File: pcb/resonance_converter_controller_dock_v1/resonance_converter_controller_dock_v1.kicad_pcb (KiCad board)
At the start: 2 copper layers, 157 parts, among them J1 FX18-120S-0.8SV15, J10 Conn_Coaxial, J11 Conn_01x02, J12 Conn_01x02, J13 Conn_Coaxial, J14 Conn_Coaxial, J15 Conn_01x02, J16 Conn_01x02, J17 Conn_Coaxial, J18 Conn_01x02, J19 Conn_01x04, J2 Conn_01x52_MountingPin, J20 Conn_01x04, J21 Conn_01x04, J22 Conn_01x06, J23 Conn_Coaxial, J24 Conn_01x02, J25 Conn_01x02, J26 Conn_Coaxial, J27 Conn_01x04, J28 Conn_01x02, J29 USB_C_Receptacle_USB2.0_14P, J3 Conn_Coaxial, J30 Conn_01x09, J31 Conn_01x04_MountingPin, J32 Conn_01x04_MountingPin, J33 Conn_01x04_MountingPin, J34 Conn_02x05_Odd_Even, J4 Conn_01x02, J5 Conn_Coaxial, J6 Conn_01x02, J7 Conn_Coaxial, J8 Conn_01x02, J9 Conn_Coaxial, M1 Fan_4pin, SW1 RotaryEncoder_Switch_MP, SW2 SW_SPST, SW3 SW_SPST, SW4 SW_SPST, SW5 SW_SPST, SW6 SW_SPST, U1 STM32F105R8Tx, U10 TMUX131RMG, U11 TMUX131RMG, U12 TMUX131RMG, U13 TMUX131RMG, U14 TMUX131RMG, U15 TMUX154ERSW, U16 AT24CS32-XHM, U17 TMUX1574RSV, U18 TMUX1574RSV, U19 TMUX131RMG, U2 FUSB302B01MPX, U20 TMUX1574RSV, U21 TMUX154ERSW, U22 TMUX154ERSW, U23 TMUX154ERSW, U24 BTS5012SDA, U25 BTS5012SDA, U26 BTS5012SDA, U27 74LVC1G04, U3 LM2576HVS-ADJ, U4 TMUX131RMG, U5 LM7812_TO220, U6 TPS2116DRL, U7 AZ1117-3.3, U8 AP2171W, U9 TMUX131RMG, Y1 16Mhz

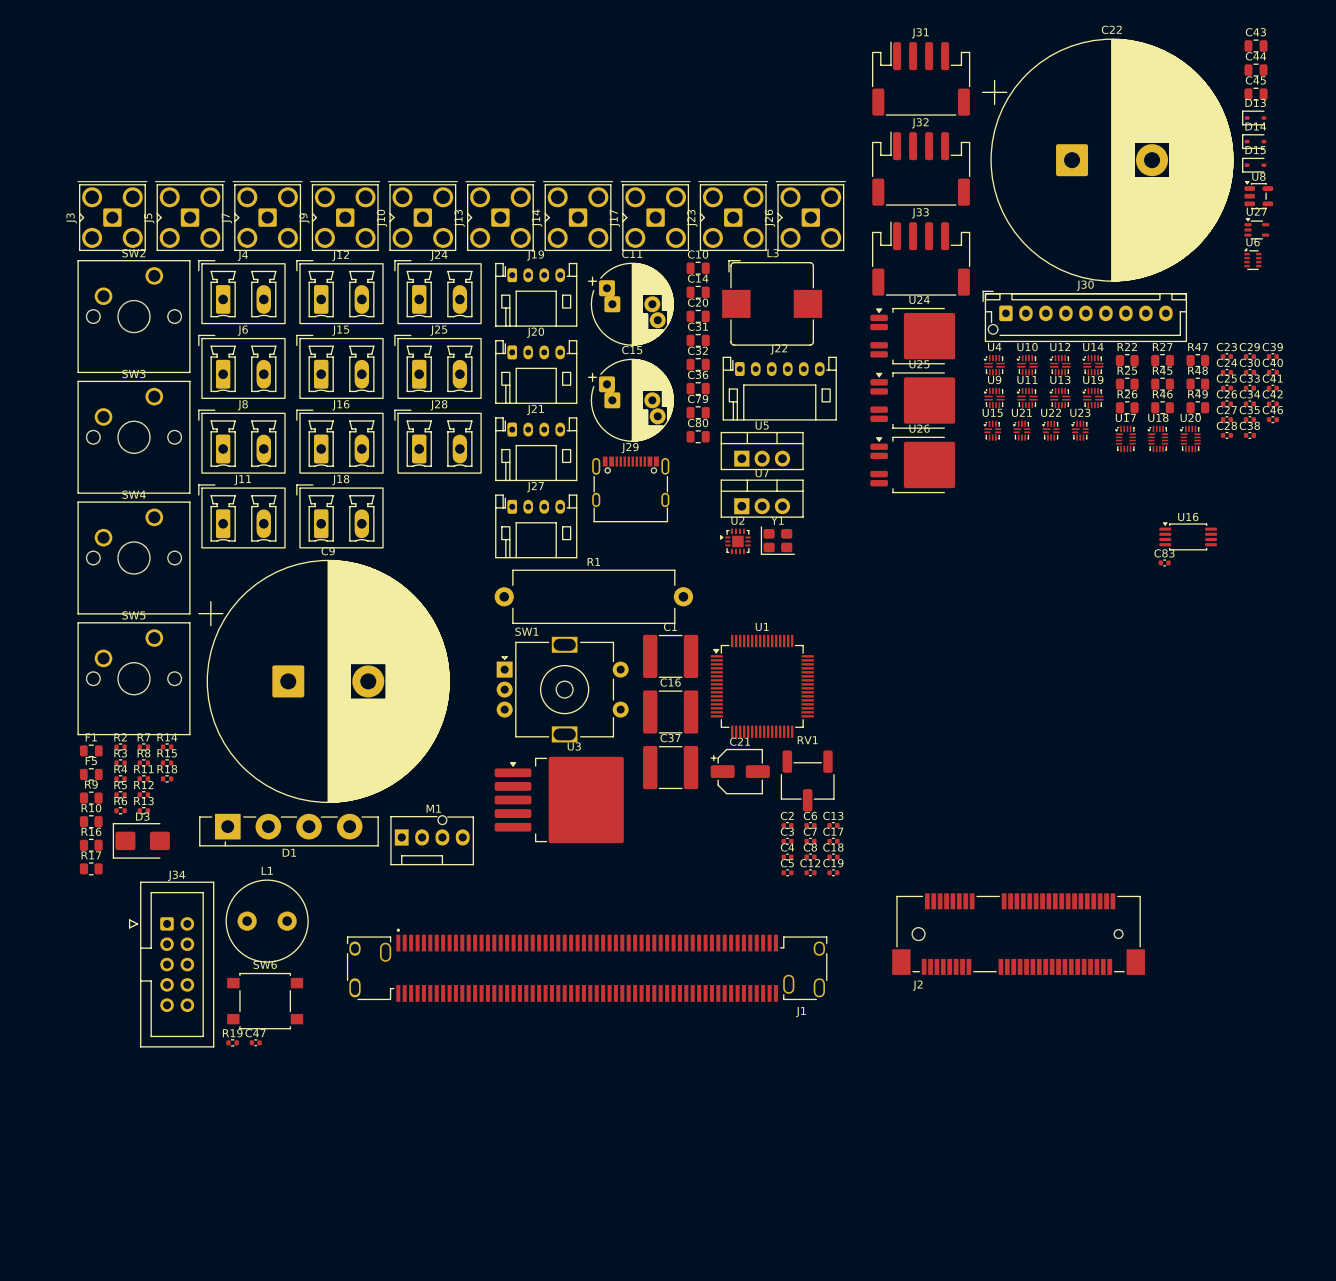
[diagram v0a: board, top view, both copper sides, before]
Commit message: Fix errors and make initial component placement in dock
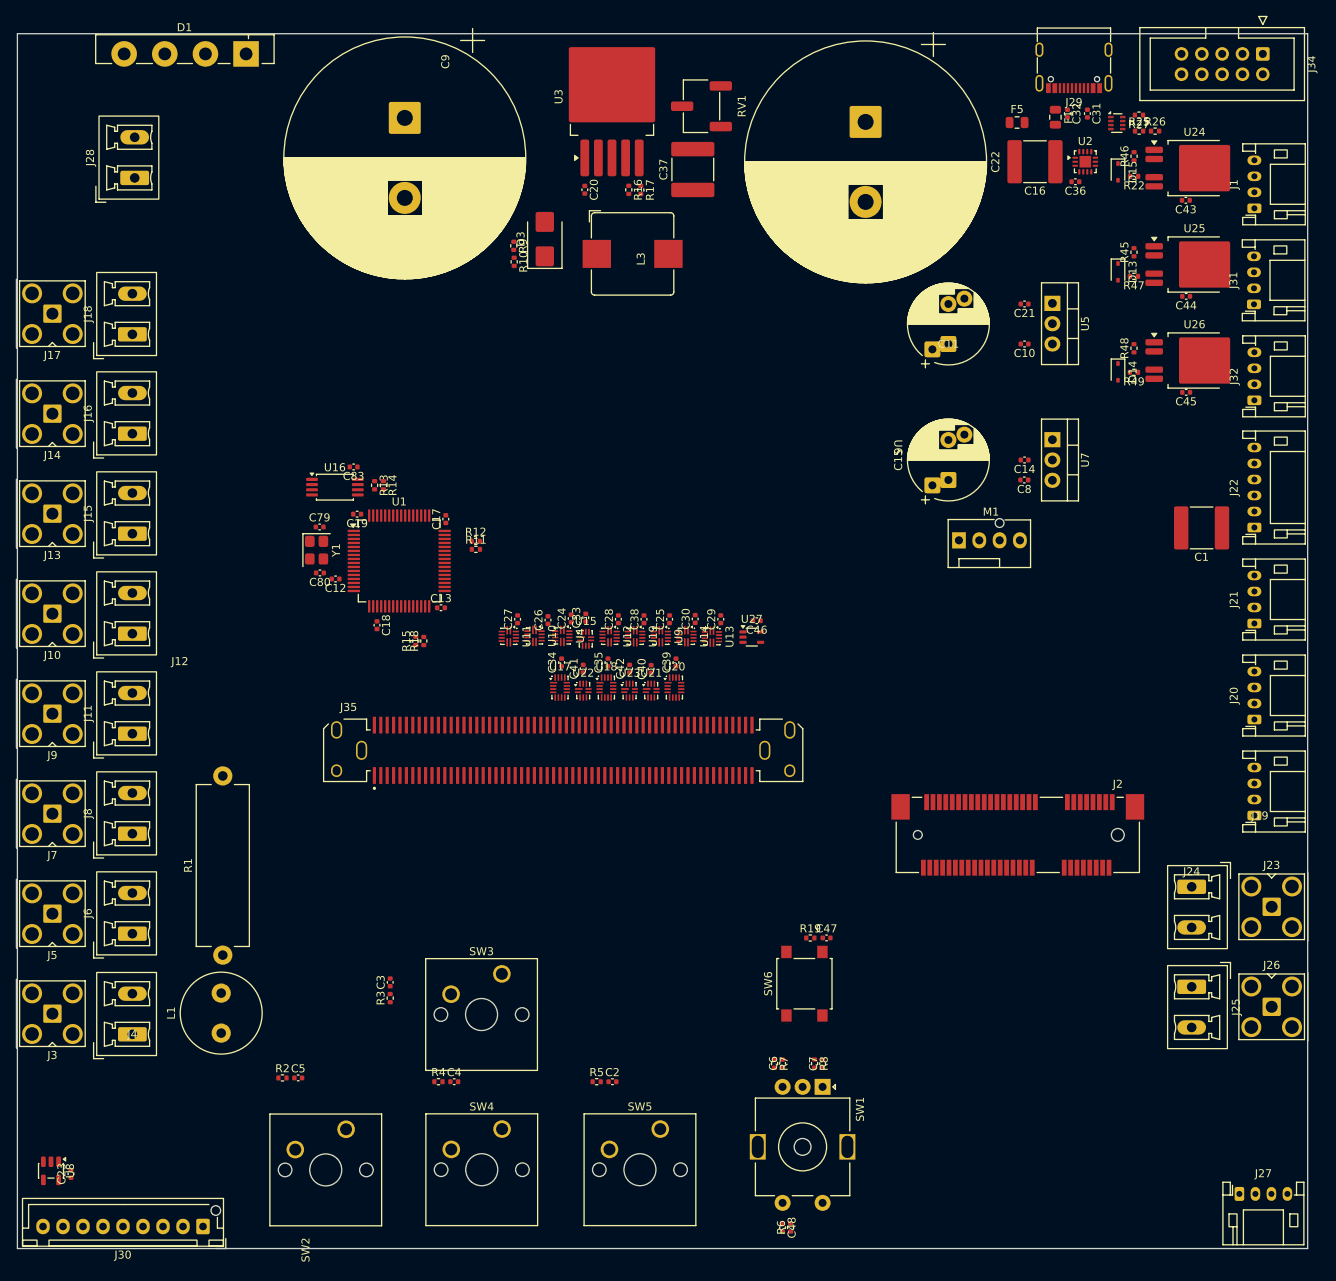
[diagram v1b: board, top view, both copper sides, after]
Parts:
- removed J33: Conn_01x04_MountingPin, Connector_JST:JST_PH_S4B-PH-SM4-TB_1x04-1MP_P2.00mm_Horizontal
- added C48: 100nF, Capacitor_SMD:C_0402_1005Metric, F.Cu at (178.8, 173.4)
- added J35: FX18-120P-0.8SV, FX18-120P-0.8SV:HIROSE_FX18-120P-0.8SV, F.Cu at (151.4, 113.7)
- C10, C14, C20, C31, C32, C36, C43, C44, C45, C79, C80: footprint Capacitor_SMD:C_0805_2012Metric -> Capacitor_SMD:C_0402_1005Metric
- C21: value C_Polarized -> C; footprint Capacitor_SMD:CP_Elec_5x4.5 -> Capacitor_SMD:C_0402_1005Metric
- C8: value 100nF -> C
- J1: value FX18-120S-0.8SV15 -> Conn_01x04; footprint FX18-120S-0.8SV15:HIROSE_FX18-120S-0.8SV15 -> Connector_JST:JST_PH_S4B-PH-K_1x04_P2.00mm_Horizontal
- J31, J32: value Conn_01x04_MountingPin -> Conn_01x04; footprint Connector_JST:JST_PH_S4B-PH-SM4-TB_1x04-1MP_P2.00mm_Horizontal -> Connector_JST:JST_PH_S4B-PH-K_1x04_P2.00mm_Horizontal
- R10, R16, R17, R22, R25, R26, R27, R45, R46, R47, R48, R49, R9: footprint Resistor_SMD:R_0805_2012Metric -> Resistor_SMD:R_0402_1005Metric
- moved U8 194.0 mm to (87.4, 166.3), turned to -90 degrees
- moved C23 177.0 mm to (89.9, 166.6), turned to 90 degrees
- moved J34 174.9 mm to (238.8, 26.6), turned to -90 degrees
- moved J30 152.0 mm to (106.4, 173.2), turned to 180 degrees
- moved F1 144.2 mm to (212.9, 34.6), turned to -90 degrees
- moved F5 141.5 mm to (208.1, 35.2)
- moved J1 126.4 mm to (237.8, 46.0), turned to 90 degrees
- moved J27 125.1 mm to (235.9, 169.2)
- moved J25 123.2 mm to (230.0, 143.3), turned to -90 degrees
- moved J24 121.3 mm to (230.0, 130.8), turned to -90 degrees
- moved J19 114.8 mm to (237.8, 121.8), turned to 90 degrees
- moved J26 114.2 mm to (240.0, 145.8), turned to -90 degrees
- moved SW2 109.3 mm to (124.3, 161.1)
- moved J23 109.3 mm to (240.0, 133.3), turned to -90 degrees
- moved R17 109.2 mm to (161.1, 43.7), turned to -90 degrees
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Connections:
- C12 pad 1: Net-(C12-Pad1) -> +3.3V
- C13 pad 1: Net-(C12-Pad1) -> +3.3V
- C17 pad 1: Net-(C12-Pad1) -> +3.3V
- C18 pad 1: Net-(C12-Pad1) -> +3.3V
- C19 pad 1: Net-(C12-Pad1) -> +3.3V
- C21 pad 1: Net-(D1-+) -> VBUS_DOCK
- C8 pad 1: Net-(D1-+) -> +12V
- J1 pad 1: GND -> Net-(J1-Pin_1)
- J1 pad 2: GND -> +3.3V
- J1 pad 3: OCD_IN -> +12V
- R45 pad 2: Net-(J32-Pin_1) -> Net-(J31-Pin_1)
- R46 pad 2: Net-(J31-Pin_1) -> Net-(J1-Pin_1)
- R48 pad 2: Net-(J33-Pin_1) -> Net-(J32-Pin_1)
- U10 pad 7: SOMLCD_SCK -> SOM_LCD_SCK
- U24 pad 1: Net-(J31-Pin_1) -> Net-(J1-Pin_1)
- U24 pad 5: Net-(J31-Pin_1) -> Net-(J1-Pin_1)
- U25 pad 1: Net-(J32-Pin_1) -> Net-(J31-Pin_1)
- U25 pad 5: Net-(J32-Pin_1) -> Net-(J31-Pin_1)
- U26 pad 1: Net-(J33-Pin_1) -> Net-(J32-Pin_1)
- U26 pad 5: Net-(J33-Pin_1) -> Net-(J32-Pin_1)
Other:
- board outline added: 161.3 x 151.8 mm

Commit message: Add mounting holes and some rework
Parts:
- added C49: C, Capacitor_SMD:C_2220_5750Metric, F.Cu at (141.8, 124.7)
- added C50: C_Polarized, Capacitor_THT:CP_Radial_D10.0mm_P5.00mm_P7.50mm, F.Cu at (115.0, 77.5)
- added C51: C, Capacitor_SMD:C_2220_5750Metric, F.Cu at (139.0, 102.4)
- added H1: MountingHole_Pad, MountingHole:MountingHole_3.2mm_M3_Pad_Via, F.Cu at (88.2, 47.6)
- added H2: MountingHole_Pad, MountingHole:MountingHole_3.2mm_M3_Pad_Via, F.Cu at (230.6, 28.5)
- added H3: MountingHole_Pad, MountingHole:MountingHole_3.2mm_M3_Pad_Via, F.Cu at (229.0, 171.0)
- added H4: MountingHole_Pad, MountingHole:MountingHole_3.2mm_M3_Pad_Via, F.Cu at (88.2, 164.3)
- added R20: R, Resistor_THT:R_Axial_Power_L20.0mm_W6.4mm_P22.40mm, F.Cu at (106.2, 140.4)
- added R21: R, Resistor_THT:R_Axial_Power_L20.0mm_W6.4mm_P22.40mm, F.Cu at (106.2, 133.3)
- U5, U7: footprint Package_TO_SOT_THT:TO-220-3_Vertical -> Package_TO_SOT_SMD:TO-263-2
- moved C47 113.2 mm to (232.8, 34.8)
- moved R19 113.2 mm to (230.8, 34.8)
- moved SW6 113.2 mm to (230.0, 40.5)
- moved R26 106.3 mm to (144.8, 105.7), turned to 90 degrees
- moved R25 106.2 mm to (144.8, 107.7), turned to 90 degrees
- moved R27 102.1 mm to (150.7, 106.0), turned to 90 degrees
- moved U6 101.7 mm to (147.9, 106.4)
- moved C79 64.8 mm to (176.3, 52.0), turned to -90 degrees
- moved Y1 64.5 mm to (173.4, 51.6), turned to 180 degrees
- moved U16 64.0 mm to (183.5, 60.3), turned to -90 degrees
- moved C80 63.3 mm to (170.5, 52.0), turned to 90 degrees
- moved C83 62.7 mm to (186.0, 62.7), turned to 90 degrees
- moved C19 58.5 mm to (177.9, 57.8), turned to 90 degrees
- moved C12 58.4 mm to (168.6, 55.9)
- moved R13 57.9 mm to (183.7, 65.3), turned to 180 degrees
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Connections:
- net Net-(U1-PA11) renamed /PUSB-
- net Net-(U1-PA12) renamed /PUSB+
- C6 pad 1: DOCK_ENCODER_CHB -> DEV_ENCODER_B
- C7 pad 1: DOCK_ENCODER_CHA -> DEV_ENCODER_A
- C8 pad 1: +12V -> VBUS_DOCK
- J27 pad 1: VCC -> +3.3V
- R2 pad 1: VCC -> +3.3V
- R3 pad 1: VCC -> +3.3V
- R4 pad 1: VCC -> +3.3V
- R5 pad 1: VCC -> +3.3V
- R6 pad 1: VCC -> +3.3V
- R7 pad 1: VCC -> +3.3V
- R7 pad 2: DOCK_ENCODER_CHB -> DEV_ENCODER_B
- R8 pad 1: VCC -> +3.3V
- R8 pad 2: DOCK_ENCODER_CHA -> DEV_ENCODER_A
- SW1 pad A: DOCK_ENCODER_CHA -> DEV_ENCODER_A
- SW1 pad B: DOCK_ENCODER_CHB -> DEV_ENCODER_B
- U1 pad 10: PAD_FWD_REMOTE -> CTRL_RXTX_FWD_REMOTE
- U1 pad 35: /PAD_BUS_SELECT_0 -> /PAD_BUS_SELECT_1
- U1 pad 36: /PAD_BUS_SELECT_1 -> /PAD_BUS_SELECT_0
- U1 pad 37: /ENCODER_BUS_SELECT_0 -> /ENCODER_BUS_SELECT_1
- U1 pad 38: /ENCODER_BUS_SELECT_1 -> /ENCODER_BUS_SELECT_0
- U1 pad 39: /LCD_BUS_SELECT_0 -> /LCD_BUS_SELECT_1
- U1 pad 40: /LCD_BUS_SELECT_1 -> /LCD_BUS_SELECT_0
- U1 pad 9: CTRL_RXTX_FWD_REMOTE -> PAD_FWD_REMOTE
- U15 pad 1: SOM_CTRL_TX -> SOM_CTRL_RX
- U15 pad 2: FROM_REMOTE_CTRL_TX -> FROM_REMOTE_CTRL_RX
- U15 pad 3: DEV_CTRL_TX -> DEV_CTRL_RX
- U15 pad 5: DEV_CTRL_RX -> DEV_CTRL_TX
- U15 pad 6: FROM_REMOTE_CTRL_RX -> FROM_REMOTE_CTRL_TX
- U15 pad 7: SOM_CTRL_RX -> SOM_CTRL_TX
- U17 pad 1: TO_REMOTE_LCD_MOSI -> TO_REMOTE_LCD_SS
- U17 pad 10: DOCK_LCD_SS -> DOCK_LCD_MOSI
- U17 pad 11: TO_REMOTE_LCD_SS -> TO_REMOTE_LCD_MOSI
- U17 pad 12: SOM_LCD_SS -> SOM_LCD_MOSI
- U17 pad 16: SOM_LCD_MOSI -> SOM_LCD_SS
- U17 pad 2: DOCK_LCD_MOSI -> DOCK_LCD_SS
- U18 pad 3: SOM_LCD_DC -> SOM_LCD_BL
- U18 pad 4: TO_REMOTE_LCD_DC -> TO_REMOTE_LCD_BL
- U18 pad 5: DOCK_LCD_DC -> DOCK_LCD_BL
- U18 pad 7: DOCK_LCD_BL -> DOCK_LCD_DC
- U18 pad 8: TO_REMOTE_LCD_BL -> TO_REMOTE_LCD_DC
- U18 pad 9: SOM_LCD_BL -> SOM_LCD_DC
- U20 pad 1: TO_REMOTE_PAD_UP -> TO_REMOTE_PAD_RIGHT
- U20 pad 10: DOCK_GPIO3 -> DOCK_GPIO0
- U20 pad 11: TO_REMOTE_PAD_RIGHT -> TO_REMOTE_PAD_UP
- U20 pad 12: SOM_PAD_RIGHT -> SOM_PAD_UP
- U20 pad 14: unconnected-(U20-VDD-Pad14) -> +3.3V
- U20 pad 16: SOM_PAD_UP -> SOM_PAD_RIGHT
- U20 pad 2: DOCK_GPIO0 -> DOCK_GPIO3
- U20 pad 3: SOM_PAD_DOWN -> SOM_PAD_LEFT
- U20 pad 4: TO_REMOTE_PAD_DOWN -> TO_REMOTE_PAD_LEFT
- U20 pad 5: DOCK_GPIO1 -> DOCK_GPIO2
- U20 pad 7: DOCK_GPIO2 -> DOCK_GPIO1
- U20 pad 8: TO_REMOTE_PAD_LEFT -> TO_REMOTE_PAD_DOWN
- U20 pad 9: SOM_PAD_LEFT -> SOM_PAD_DOWN
- U22 pad 1: SOM_CTRL_TX -> SOM_CTRL_RX
- U22 pad 2: TO_REMOTE_CTRL_TX -> TO_REMOTE_CTRL_RX
- U22 pad 3: DOCK_CTRL_TX -> DOCK_CTRL_RX
- U22 pad 5: DOCK_CTRL_RX -> DOCK_CTRL_TX
- U22 pad 6: TO_REMOTE_CTRL_RX -> TO_REMOTE_CTRL_TX
- U22 pad 7: SOM_CTRL_RX -> SOM_CTRL_TX
- U7 pad 3: +12V -> VBUS_DOCK
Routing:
- net VBUS_DOCK: track 0.00 -> 284.1 mm, vias 0 -> 5
- net VOUT: track 0.00 -> 224.2 mm, vias 0 -> 2
- net GND: track 0.00 -> 195.3 mm, vias 0 -> 164
- net DEV_PAD_CENTER: track 0.00 -> 190.1 mm, vias 0 -> 2
- net DEV_ENCODER_B: track 0.00 -> 175.3 mm, vias 0 -> 2
- net DEV_ENCODER_A: track 0.00 -> 173.2 mm, vias 0 -> 2
- net DEV_PAD_RIGHT: track 0.00 -> 169.4 mm, vias 0 -> 2
- net DEV_PAD_DOWN: track 0.00 -> 157.3 mm, vias 0 -> 2
- net DEV_LCD_RST: track 0.00 -> 153.9 mm, vias 0 -> 2
- net INT_VCC: track 0.00 -> 142.2 mm, vias 0 -> 2
- net INTERNAL_I2C_SDA: track 0.00 -> 140.3 mm, vias 0 -> 3
- net INTERNAL_I2C_SCL: track 0.00 -> 139.4 mm, vias 0 -> 2
- net DEV_PAD_LEFT: track 0.00 -> 137.9 mm, vias 0 -> 2
- net DEV_PAD_UP: track 0.00 -> 136.7 mm, vias 0 -> 2
- net DEV_LCD_DC: track 0.00 -> 136.3 mm, vias 0 -> 2
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- added copper zone on In2.Cu, net +3.3V
- added copper zone on In1.Cu, net GND
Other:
- copper layers 2 -> 4
